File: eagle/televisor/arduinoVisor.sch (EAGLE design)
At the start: 23 parts

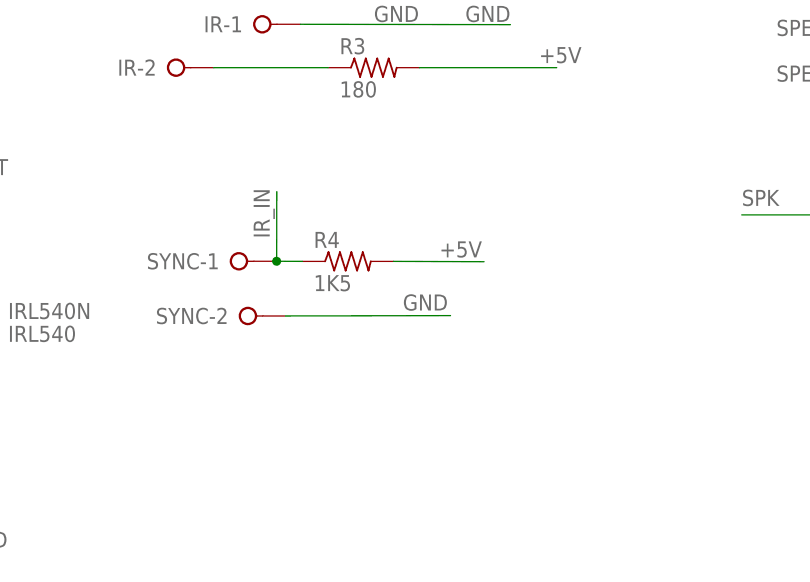
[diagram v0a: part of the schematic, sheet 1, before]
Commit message: board IR swap pins. ground planes. code uncrustified.
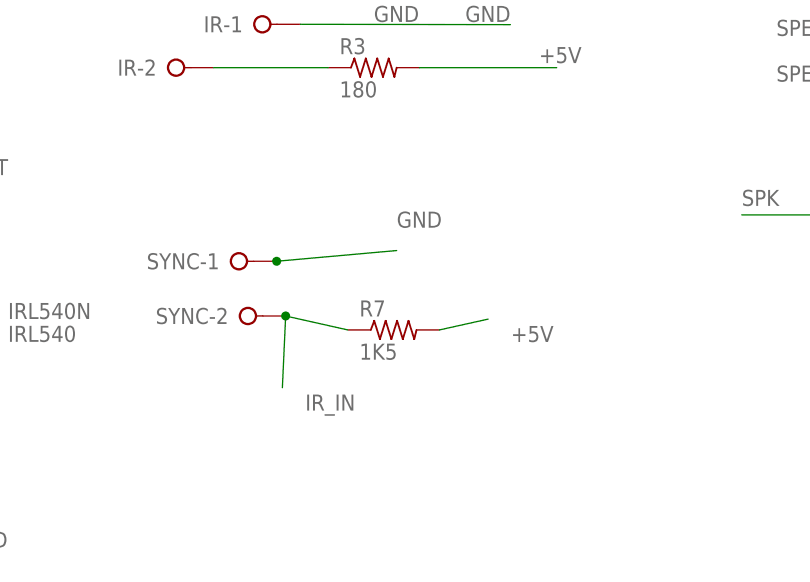
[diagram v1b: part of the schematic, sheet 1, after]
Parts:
- removed R4: 1K5, rcl:R-US_0207/10
- added R7: 1K5, rcl:R-US_0207/10
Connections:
- net +5V: now also R7.2; no longer R4.2
- net GND: now also SYNC-1.KL; no longer SYNC-2.KL
- net IR_IN: now also R7.1, SYNC-2.KL; no longer R4.1, SYNC-1.KL
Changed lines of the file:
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@@
 <part name="LED" library="con-wago-508" deviceset="W237-02P" device=""/>
 <part name="LCD" library="pinhead" deviceset="PINHD-1X4" device=""/>
-<part name="R4" library="rcl" deviceset="R-US_" device="0207/10" value="1K5"/>
 <part name="PCB2" library="E14_Arduino_revC 2 boo" deviceset="ARDUINO_MICRO" device=""/>
 <part name="IRL540N" library="transistor-power" deviceset="IRF540" device="" value="IRL540"/>
@@
 <part name="R6" library="rcl" deviceset="R-US_" device="0207/10" value="10K"/>
 <part name="R2" library="rcl" deviceset="R-US_" device="0207/10" value="10K"/>
+<part name="R7" library="rcl" deviceset="R-US_" device="0207/10" value="1K5"/>
 </parts>
 <sheets>
@@
 <attribute name="VALUE" x="-1.27" y="48.26" size="1.778" layer="96"/>
 </instance>
-<instance part="R4" gate="G$1" x="136.824146875" y="-3.743184375" smashed="yes">
-<attribute name="NAME" x="133.014146875" y="-2.244584375" size="1.778" layer="95"/>
-<attribute name="VALUE" x="133.014146875" y="-7.045184375" size="1.778" layer="96"/>
-</instance>
 <instance part="PCB2" gate="G$1" x="127" y="127" smashed="yes" rot="R90"/>
 <instance part="IRL540N" gate="G$1" x="91.43743125" y="-12.684190625" smashed="yes">
@@
 <attribute name="NAME" x="161.0614" y="69.85" size="1.778" layer="95" rot="R90"/>
 <attribute name="VALUE" x="165.862" y="69.85" size="1.778" layer="96" rot="R90"/>
+</instance>
+<instance part="R7" gate="G$1" x="141.904146875" y="-11.363184375" smashed="yes">
+<attribute name="NAME" x="138.094146875" y="-9.864584375" size="1.778" layer="95"/>
+<attribute name="VALUE" x="138.094146875" y="-14.665184375" size="1.778" layer="96"/>
 </instance>
 </instances>
@@
 </segment>
 <segment>
-<pinref part="SYNC" gate="-2" pin="KL"/>
-<wire x1="129.904146875" y1="-9.810703125" x2="148.22059375" y2="-9.768" width="0.1524" layer="91"/>
-<label x="142.916021875" y="-9.203140625" size="1.778" layer="95"/>
-</segment>
-<segment>
 <pinref part="IRL540" gate="G$1" pin="S"/>
 <wire x1="17.82" y1="-22.86" x2="18.4" y2="-22.28" width="0.1524" layer="91"/>
@@
 <wire x1="78.74" y1="-35.56" x2="78.74" y2="-43.18" width="0.1524" layer="91"/>
 <wire x1="78.74" y1="-33.02" x2="78.74" y2="-35.56" width="0.1524" layer="91"/>
+</segment>
+<segment>
+<pinref part="SYNC" gate="-1" pin="KL"/>
+<wire x1="128.904146875" y1="-3.730703125" x2="128.944146875" y2="-3.770703125" width="0.1524" layer="91"/>
+<wire x1="128.904146875" y1="-3.730703125" x2="142.24" y2="-2.54" width="0.1524" layer="91"/>
+<junction x="128.904146875" y="-3.730703125"/>
+<label x="142.24" y="0" size="1.778" layer="95"/>
 </segment>
 </net>
@@
 <net name="IR_IN" class="0">
 <segment>
-<pinref part="SYNC" gate="-1" pin="KL"/>
-<wire x1="128.904146875" y1="-3.730703125" x2="128.944146875" y2="-3.770703125" width="0.1524" layer="91"/>
-<pinref part="R4" gate="G$1" pin="1"/>
-<wire x1="128.904146875" y1="-3.730703125" x2="131.744146875" y2="-3.743184375" width="0.1524" layer="91"/>
-<junction x="128.904146875" y="-3.730703125"/>
-<wire x1="128.904146875" y1="-3.730703125" x2="128.9209875" y2="4.014590625" width="0.1524" layer="91"/>
-<label x="128.13094375" y="-1.182121875" size="1.778" layer="95" rot="R90"/>
-</segment>
-<segment>
 <pinref part="PCB2" gate="G$1" pin="D7"/>
 <wire x1="111.76" y1="121.92" x2="91.44" y2="121.92" width="0.1524" layer="91"/>
 <label x="91.44" y="121.92" size="1.778" layer="95"/>
 </segment>
+<segment>
+<pinref part="R7" gate="G$1" pin="1"/>
+<pinref part="SYNC" gate="-2" pin="KL"/>
+<wire x1="136.824146875" y1="-11.363184375" x2="129.904146875" y2="-9.810703125" width="0.1524" layer="91"/>
+<wire x1="129.54" y1="-17.78" x2="129.904146875" y2="-9.810703125" width="0.1524" layer="91"/>
+<junction x="129.904146875" y="-9.810703125"/>
+<label x="132.08" y="-20.32" size="1.778" layer="95"/>
+</segment>
 </net>
 <net name="+5V" class="0">
-<segment>
-<pinref part="R4" gate="G$1" pin="2"/>
-<wire x1="141.904146875" y1="-3.743184375" x2="151.94508125" y2="-3.78048125" width="0.1524" layer="91"/>
-<label x="151.719353125" y="-1.521040625" size="1.778" layer="95" rot="R180"/>
-</segment>
 <segment>
 <pinref part="R3" gate="G$1" pin="2"/>
@@
 <label x="-17.814209375" y="60.85823125" size="1.778" layer="95" rot="R180" xref="yes"/>
 </segment>
-</net>
+<segment>
+<pinref part="R7" gate="G$1" pin="2"/>
+<wire x1="146.984146875" y1="-11.363184375" x2="152.4" y2="-10.16" width="0.1524" layer="91"/>
+<label x="154.94" y="-12.7" size="1.778" layer="95"/>
+</segment>
+</net>
